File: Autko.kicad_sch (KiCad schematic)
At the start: 0 parts

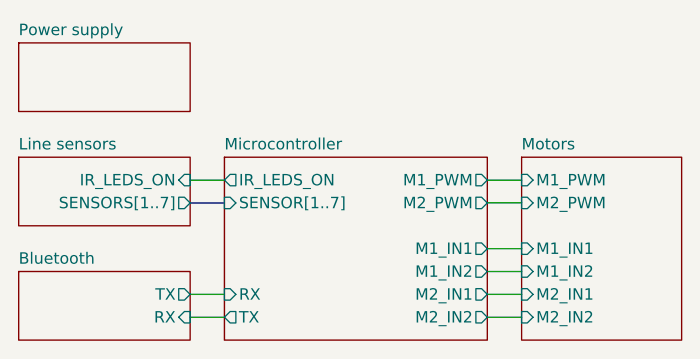
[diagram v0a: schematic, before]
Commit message: Line sensors
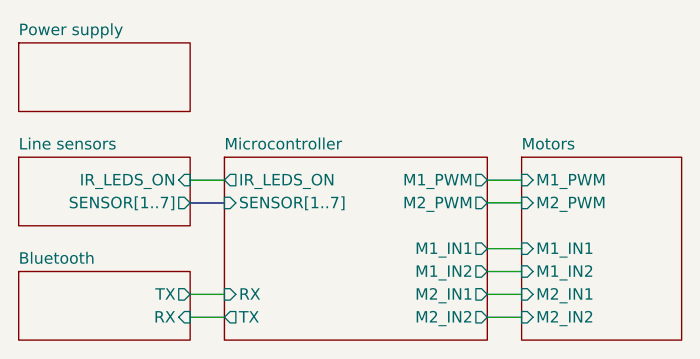
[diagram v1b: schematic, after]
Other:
- sheet Line sensors ports: added SENSOR[1..7]; removed SENSORS[1..7]
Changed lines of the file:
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@@
       (effects (font (size 1.27 1.27)) (justify right))
     )
-    (pin "SENSORS[1..7]" output (at 43.18 43.18 0)
+    (pin "SENSOR[1..7]" output (at 43.18 43.18 0)
       (effects (font (size 1.27 1.27)) (justify right))
     )
